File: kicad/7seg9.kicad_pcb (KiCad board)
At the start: 2 copper layers, 103 x 20.3 mm, 16 parts, among them J1 PMOD_01x06, U1 SGM6603-5.0, U2 TM1640

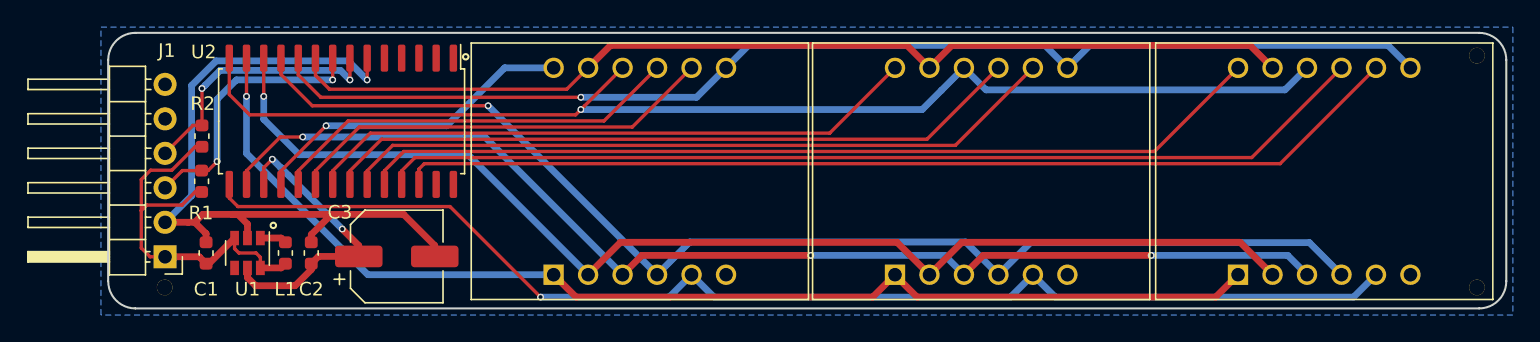
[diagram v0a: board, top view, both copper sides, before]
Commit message: Kicad and OSS toolchain version upgrades
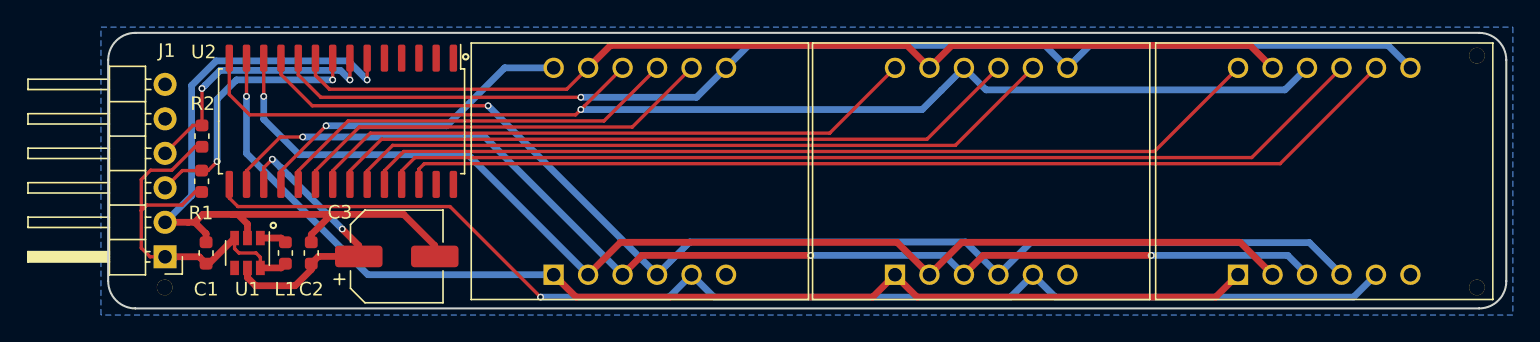
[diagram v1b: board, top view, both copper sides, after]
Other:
- net class 0.25 SMD removed
- net class Default removed
